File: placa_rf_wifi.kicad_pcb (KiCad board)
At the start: 2 copper layers, 9 parts

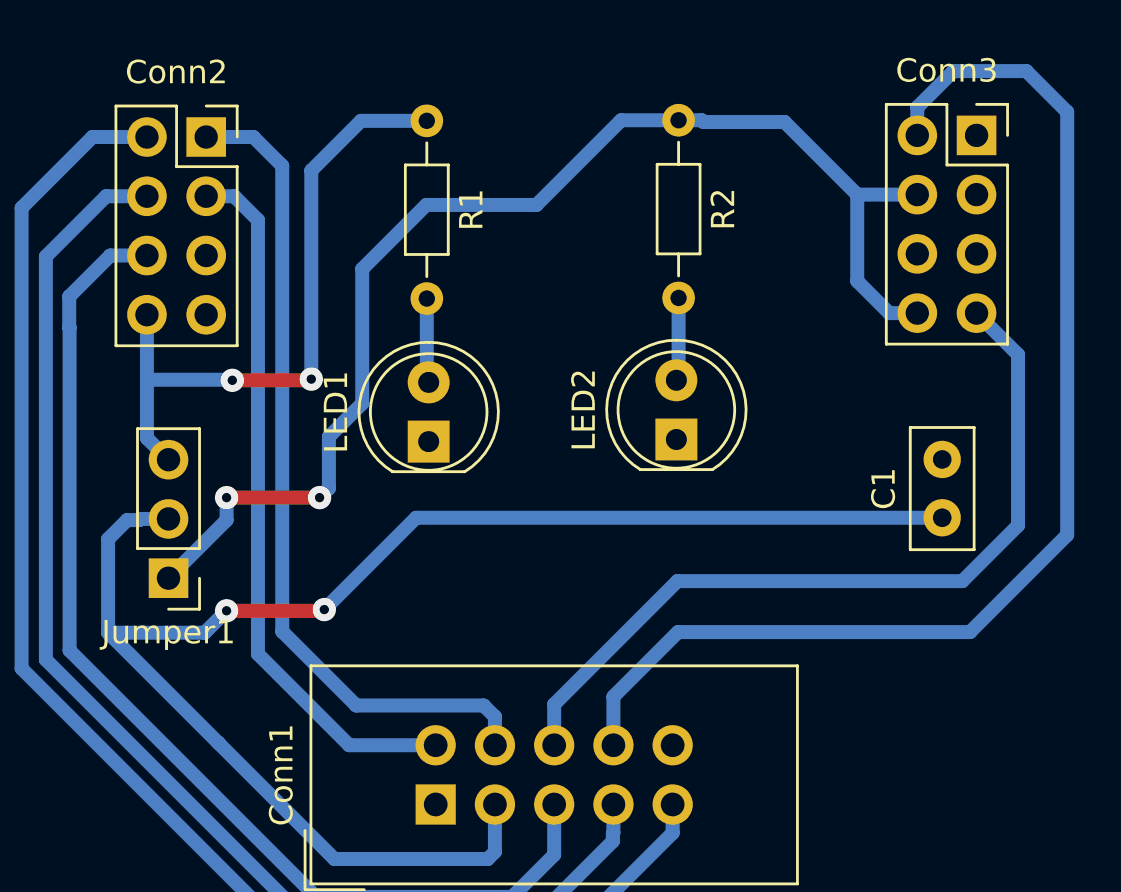
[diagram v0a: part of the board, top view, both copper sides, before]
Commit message: Se trasladaron los pines de 2 a 10, inconvenientes con GND
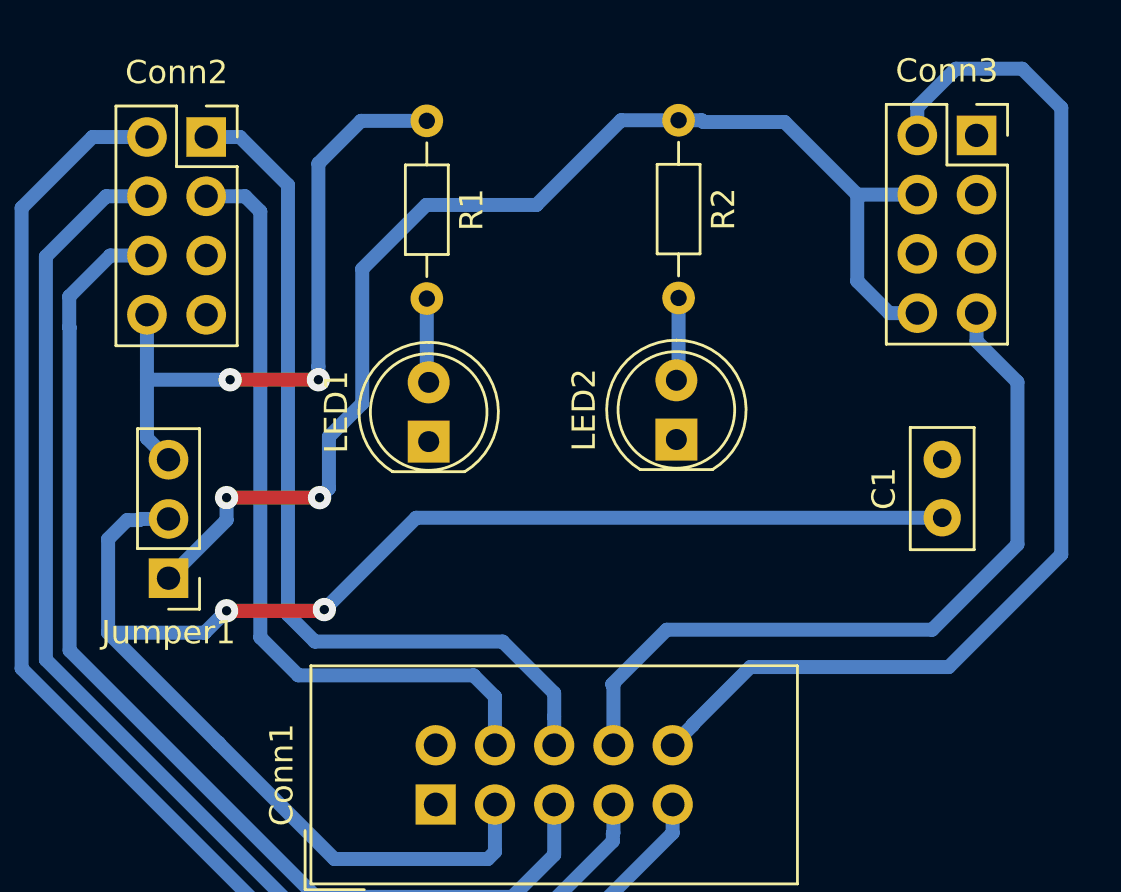
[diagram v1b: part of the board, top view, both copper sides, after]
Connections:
- Conn1 pad 10: Net-(Conn1-Pad10) -> TX
- Conn1 pad 2: SCK -> Net-(Conn1-Pad2)
- Conn1 pad 4: MISO -> SCK
- Conn1 pad 6: RX -> MISO
- Conn1 pad 8: TX -> RX
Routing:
- net TX: track 51.5 -> 48.0 mm
- net SCK: track 30.5 -> 34.0 mm
- net MISO: track 35.6 -> 37.8 mm
- net RX: track 34.7 -> 33.1 mm

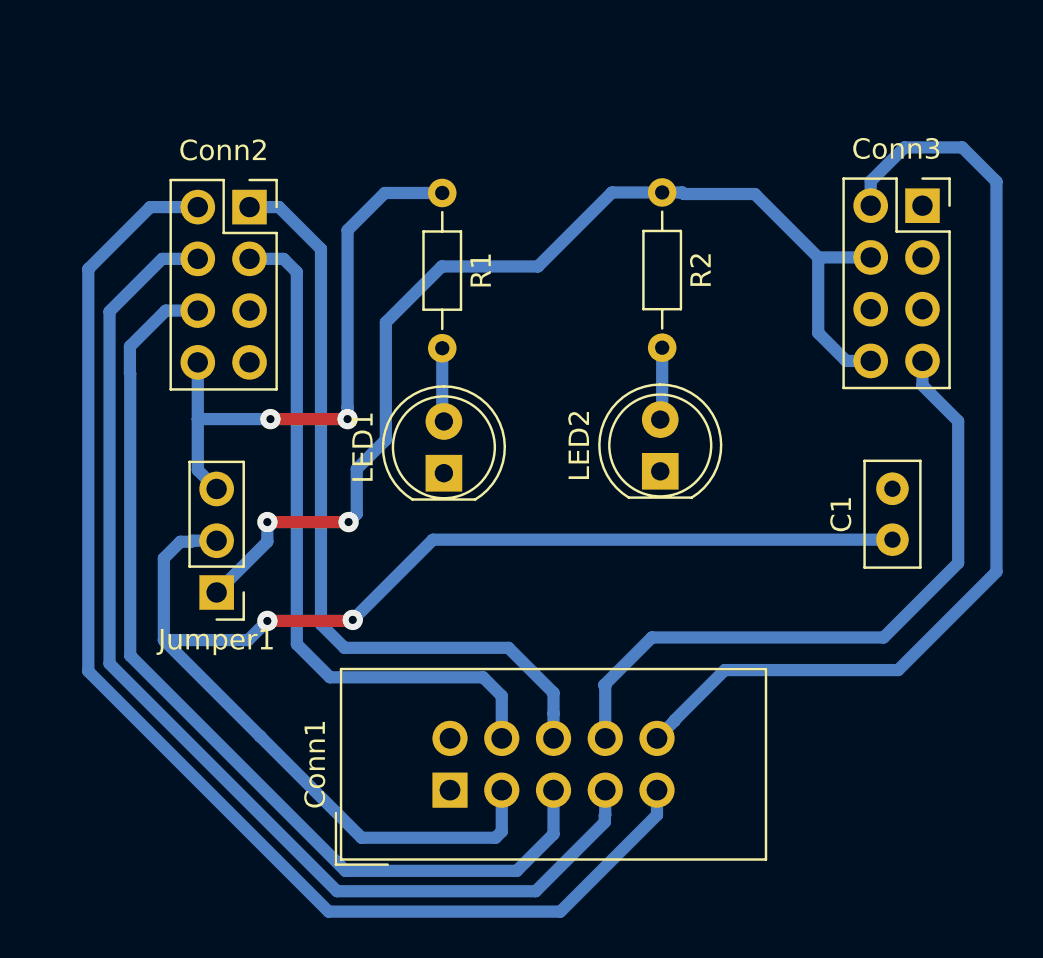
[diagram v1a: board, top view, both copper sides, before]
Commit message: Version de la placa simplificada, con un solo LED
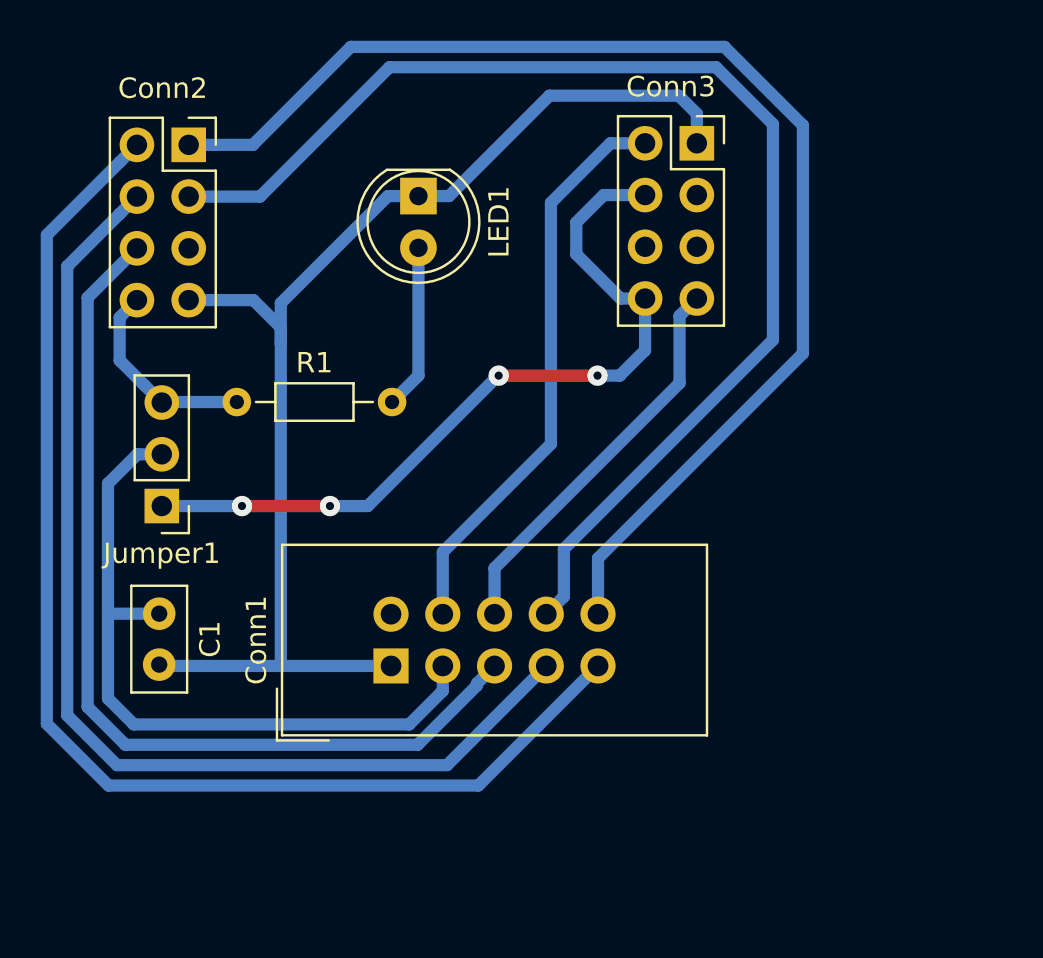
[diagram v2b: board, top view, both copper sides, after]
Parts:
- removed LED2: D_Wifi, LED_THT:LED_D5.0mm
- removed R2: R_Wifi, Resistor_THT:R_Axial_DIN0204_L3.6mm_D1.6mm_P7.62mm_Horizontal
- moved C1 36.2 mm to (128.0, 98.2), turned to 270 degrees
- moved R1 14.4 mm to (131.8, 87.8), turned to 0 degrees
- moved LED1 13.7 mm to (140.7, 77.7), turned to 270 degrees
- moved Conn3 11.5 mm to (154.4, 75.1)
- moved Conn1 6.75 mm to (139.4, 100.8)
- moved Jumper1 5.02 mm to (128.1, 92.9)
- moved Conn2 4.27 mm to (129.5, 75.2)
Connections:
- Conn1 pad 10: TX -> MISO
- Conn1 pad 4: SCK -> TX
- Conn1 pad 6: MISO -> RX
- Conn1 pad 8: RX -> SCK
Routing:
- net GND: track 0.00 -> 61.6 mm
- net +3V3: track 67.6 -> 35.2 mm, vias 2 -> 0
- net SCK: track 34.0 -> 61.1 mm
- net MISO: track 37.8 -> 61.9 mm
- net TX: track 48.0 -> 28.2 mm
- net VccRF: track 28.6 -> 9.93 mm, vias 2 -> 0
- net VccWifi: track 53.6 -> 39.2 mm, vias 2 -> 4
- net RX: track 33.1 -> 19.6 mm
- net Net-(LED1-Pad2): track 3.63 -> 8.11 mm
- net Net-(LED2-Pad2): track 3.61 -> 0.00 mm
- net CSN: track 47.3 -> 45.9 mm
- net IRQ: track 62.4 -> 61.0 mm
- net MOSI: track 54.6 -> 53.4 mm

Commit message: Placa completa, ordenada, doble capa
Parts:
- added LED2: D_Wifi, LED_THT:LED_D5.0mm, F.Cu at (149.0, 75.7)
- added R2: R_Wifi, Resistor_THT:R_Axial_DIN0204_L3.6mm_D1.6mm_P7.62mm_Horizontal, F.Cu at (149.1, 90.0)
- moved Jumper1 18.9 mm to (147.0, 94.0), turned to 270 degrees
- moved Conn3 7.80 mm to (162.2, 74.9)
- moved R1 7.31 mm to (138.7, 90.2), turned to 90 degrees
- moved C1 6.35 mm to (128.5, 91.9)
- moved Conn1 3.14 mm to (140.2, 103.8)
- moved LED1 2.80 mm to (138.7, 75.7)
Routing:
- net GND: track 61.6 -> 0.00 mm
- net SCK: track 61.1 -> 96.8 mm
- net MISO: track 61.9 -> 79.7 mm
- net VccWifi: track 39.2 -> 28.1 mm, vias 4 -> 0
- net VccRF: track 9.93 -> 20.7 mm
- net +3V3: track 35.2 -> 42.9 mm
- net RX: track 19.6 -> 25.8 mm
- net TX: track 28.2 -> 33.4 mm
- net Net-(LED2-Pad2): track 0.00 -> 4.17 mm
- net Net-(LED1-Pad2): track 8.11 -> 4.29 mm
- net CSN: track 45.9 -> 48.1 mm
- net MOSI: track 53.4 -> 55.0 mm
- net IRQ: track 61.0 -> 62.2 mm
- added copper zone on B.Cu, net GND

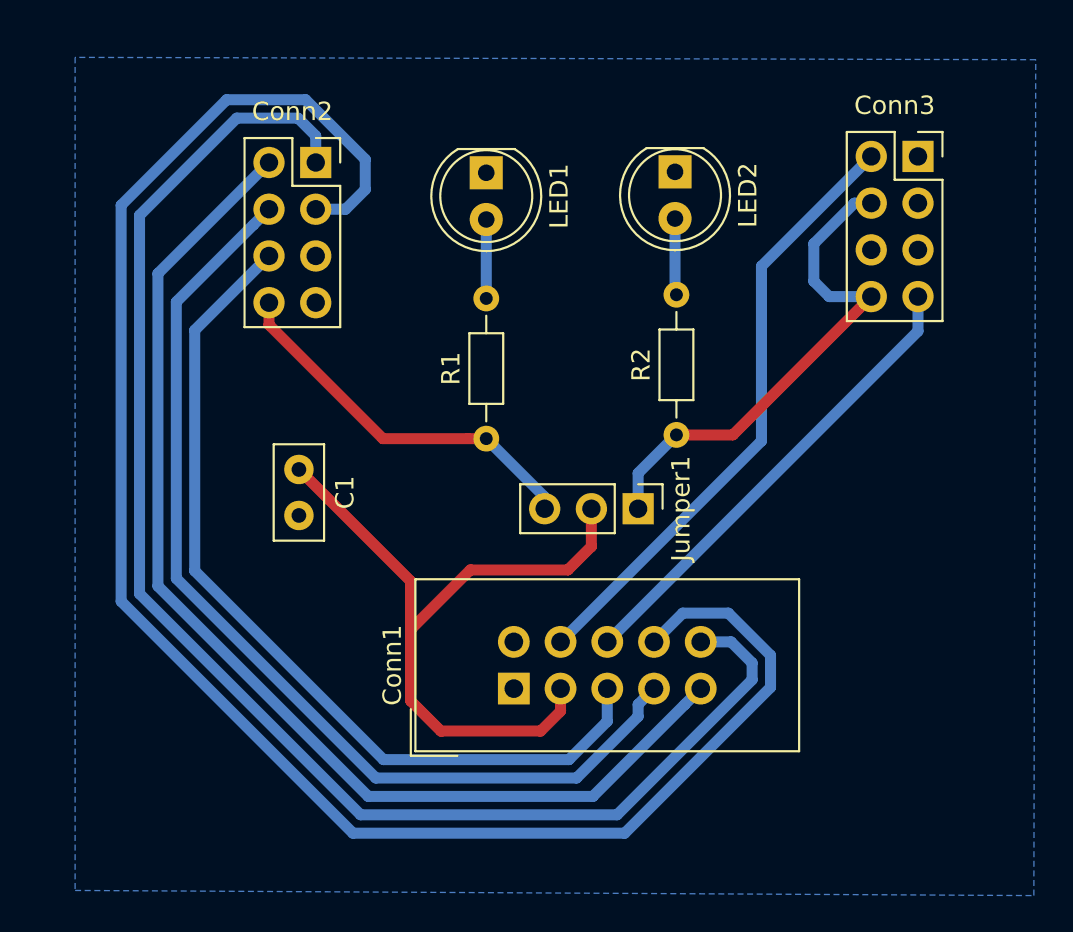
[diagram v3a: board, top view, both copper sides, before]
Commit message: Placa simplificada II, un solo puente
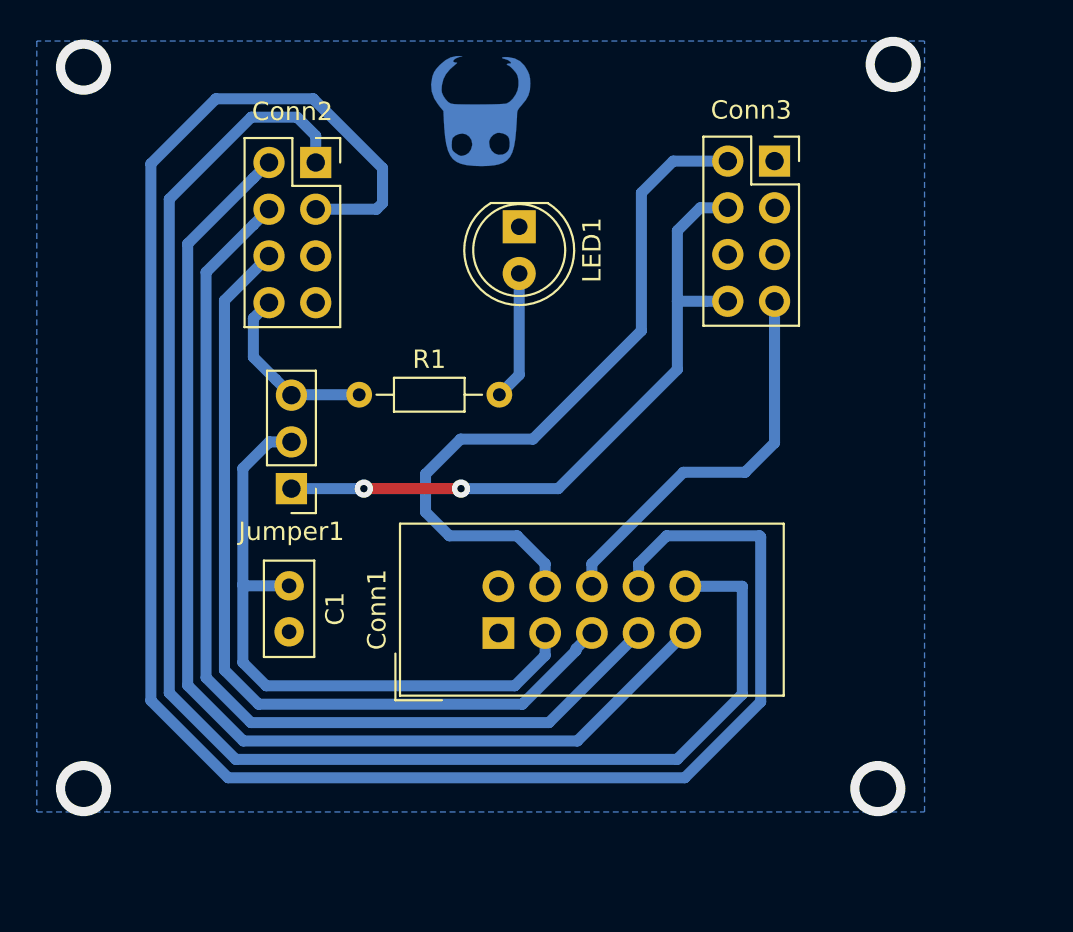
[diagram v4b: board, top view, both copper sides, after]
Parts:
- removed LED2: D_Wifi, LED_THT:LED_D5.0mm
- removed R2: R_Wifi, Resistor_THT:R_Axial_DIN0204_L3.6mm_D1.6mm_P7.62mm_Horizontal
- added ?: , Logos:Logo_Cobre, F.Cu at (138.4, 72.4)
- moved Jumper1 18.9 mm to (128.1, 92.9), turned to 180 degrees
- moved Conn3 7.80 mm to (154.4, 75.1)
- moved R1 7.31 mm to (131.8, 87.8), turned to 0 degrees
- moved C1 6.35 mm to (128.0, 98.2)
- moved LED1 3.44 mm to (140.5, 78.7)
- moved Conn1 3.14 mm to (139.4, 100.8)
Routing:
- net VccRF: track 20.7 -> 9.93 mm
- net VccWifi: track 28.1 -> 37.2 mm, vias 0 -> 2
- net SCK: track 96.8 -> 104.6 mm
- net +3V3: track 42.9 -> 35.2 mm
- net TX: track 33.4 -> 38.8 mm
- net RX: track 25.8 -> 21.6 mm
- net Net-(LED2-Pad2): track 4.17 -> 0.00 mm
- net Net-(LED1-Pad2): track 4.29 -> 7.11 mm
- net CSN: track 48.1 -> 45.9 mm
- net MISO: track 79.7 -> 81.6 mm
- net MOSI: track 55.0 -> 53.4 mm
- net IRQ: track 62.2 -> 61.0 mm
- net (no net): vias 0 -> 4

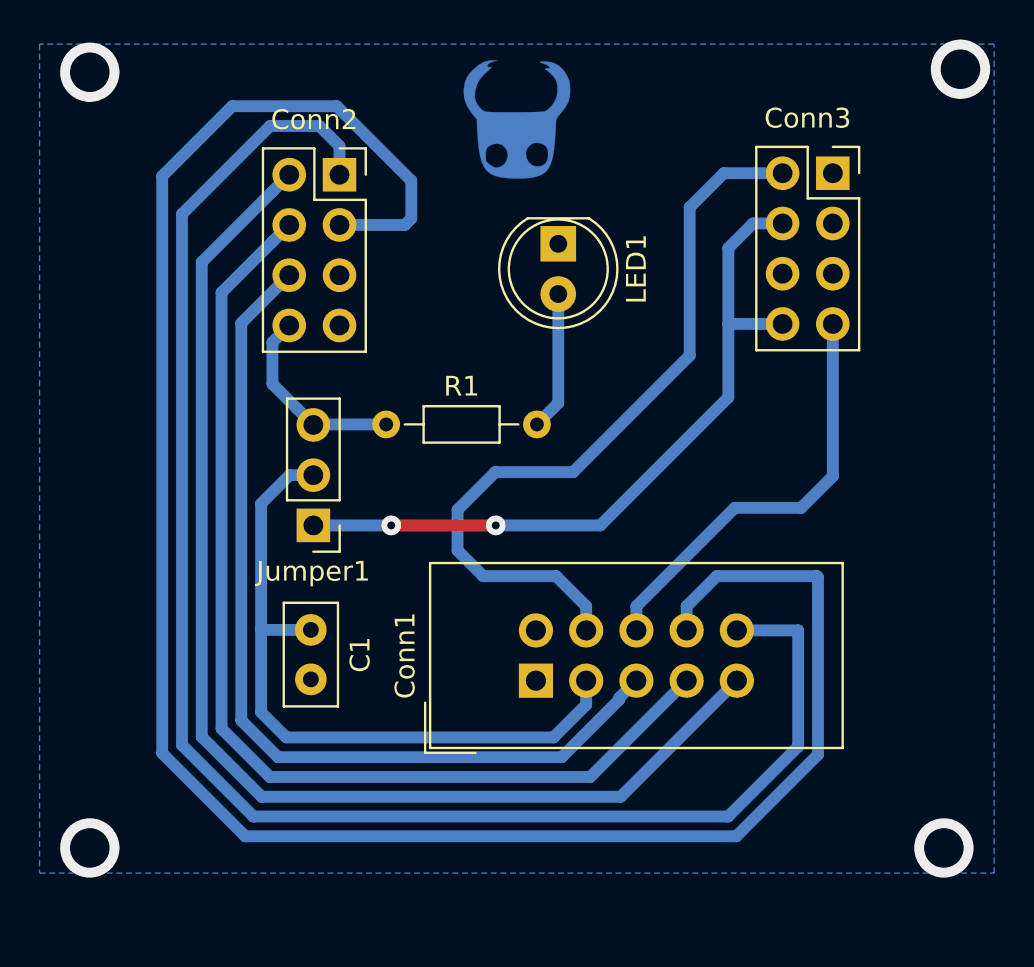
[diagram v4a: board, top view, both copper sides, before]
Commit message: Placa simplificada II, nueva disposicion de pines
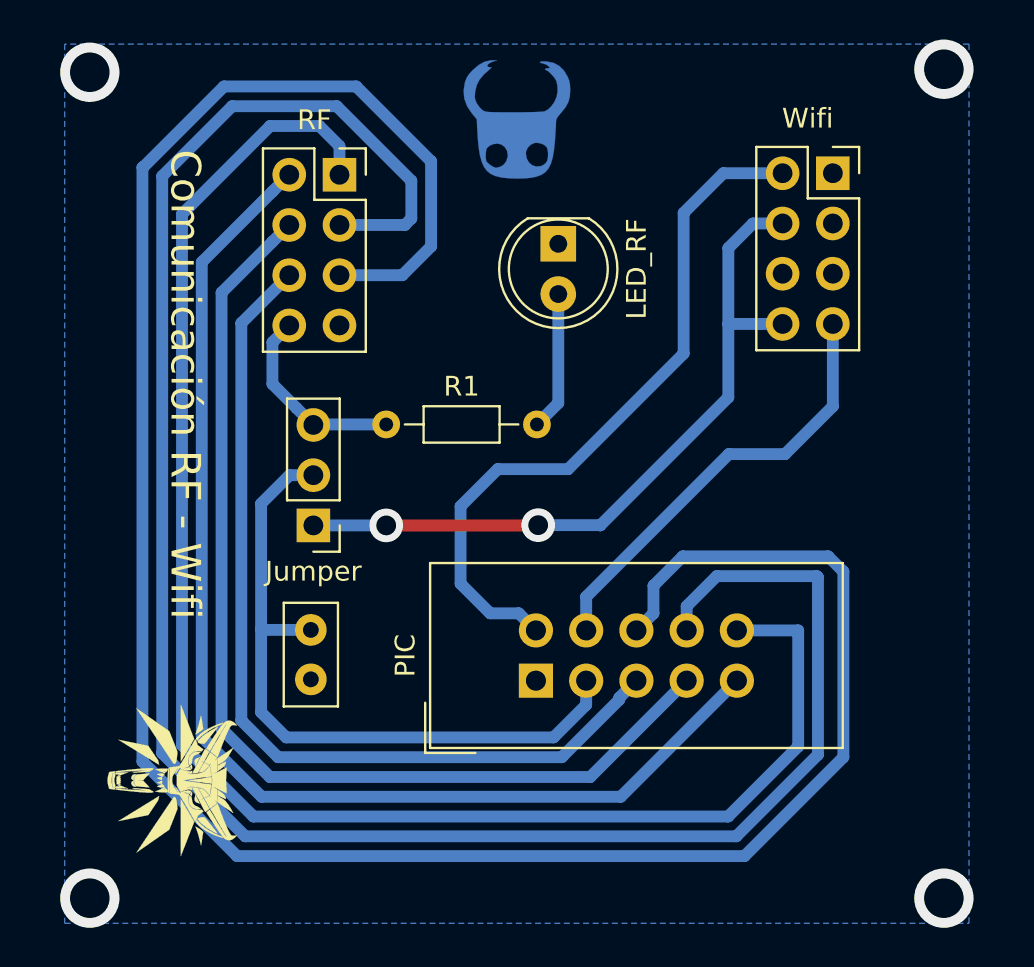
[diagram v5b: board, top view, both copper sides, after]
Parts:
- added ?: , Logos:Witcher2, F.Cu at (121.0, 105.8)
- renumbered C1 to ?, Jumper1 to Jumper, LED1 to LED_RF, Conn1 to PIC, Conn2 to RF, Conn3 to Wifi
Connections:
- PIC pad 2: Net-(Conn1-Pad2) -> TX
- PIC pad 4: TX -> RX
- PIC pad 6: RX -> CE
- RF pad 6: Net-(Conn2-Pad6) -> CE
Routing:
- net CE: track 0.00 -> 119.5 mm
- net TX: track 38.8 -> 36.1 mm
- net RX: track 21.6 -> 22.3 mm
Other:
- board text added: "Comunicación RF - Wifi"

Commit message: Placa simplificada II, sin IRQ y sin uso del RB8
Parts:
- gave numbers to parts that had none: 1
- renumbered PIC to Conn1, RF to Conn2, Wifi to Conn3, Jumper to Jumper1, LED_RF to LED1
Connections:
- Conn1 pad 10: MISO -> SCK
- Conn1 pad 2: TX -> Net-(Conn1-Pad2)
- Conn1 pad 4: RX -> TX
- Conn1 pad 6: CE -> RX
- Conn1 pad 8: SCK -> CE
- Conn1 pad 9: IRQ -> MISO
- Conn2 pad 1: IRQ -> Net-(Conn2-Pad1)
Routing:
- net IRQ: track 61.0 -> 0.00 mm
- net MISO: track 81.6 -> 70.3 mm
- net SCK: track 104.6 -> 95.1 mm
- net CE: track 119.5 -> 113.1 mm
- net TX: track 36.1 -> 38.6 mm
